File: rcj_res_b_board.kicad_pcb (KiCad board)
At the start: 2 copper layers, 82 x 100 mm, 50 parts, among them P1 M0_TERM, P10 PING0, P11 MPU9250, P12 SERVO0, P2 M1_TERM, P3 GP2Y0A41SK0F, P4 GP2Y0A41SK0F, P5 GP2Y0A41SK0F, P6 GP2Y0A41SK0F, P7 GP2Y0A21YK, P8 GP2Y0A21YK, P9 GP2Y0A21YK

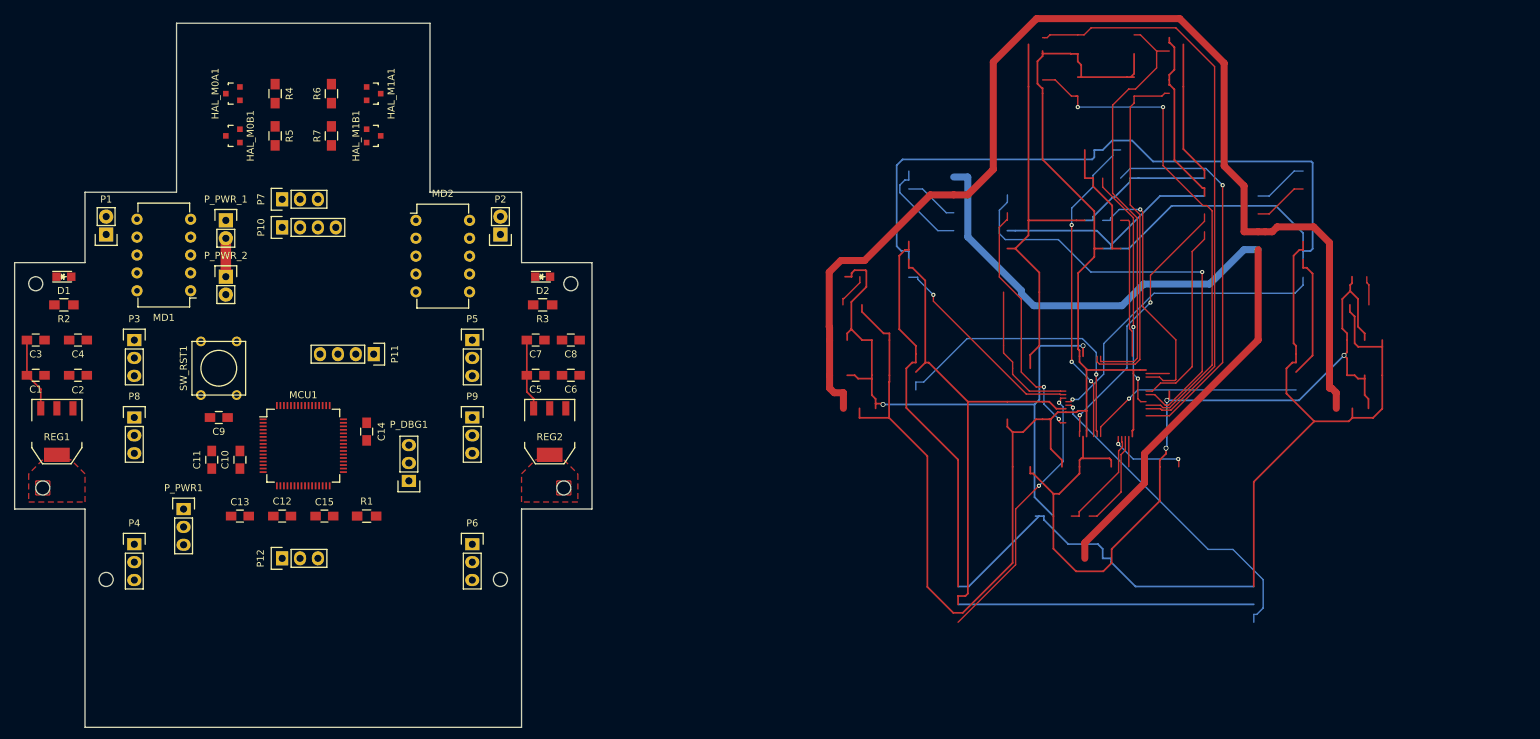
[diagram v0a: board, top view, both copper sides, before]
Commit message: Moved SMD components to back
Moving components to back to free up space -
fewer physical obstacles / limitations
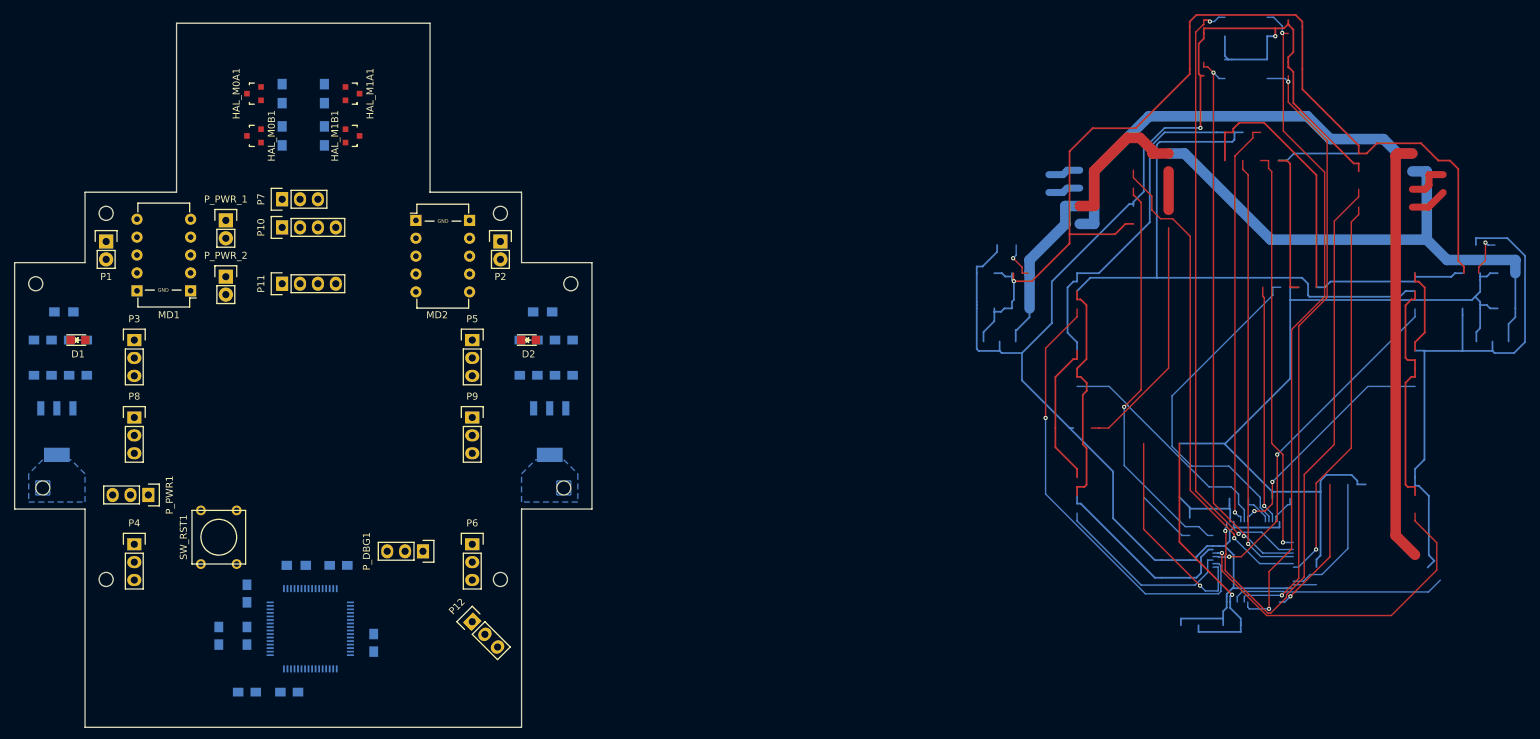
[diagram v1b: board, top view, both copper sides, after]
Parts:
- C1, C10, C11, C12, C13, C14, C15, C2, C3, C4, C5, C6, C7, C8, C9, MCU1, R1, R2, R3, R4, R5, R6, R7, REG1, REG2: moved to B.Cu
- moved C14 30.0 mm to (71.0, 138.0), turned to 90 degrees
- moved P12 28.5 mm to (85.0, 135.0), turned to 45 degrees
- moved MCU1 26.0 mm to (62.0, 136.0)
- moved C9 25.3 mm to (53.0, 131.0), turned to 90 degrees
- moved C10 25.0 mm to (53.0, 137.0), turned to 270 degrees
- moved C11 25.0 mm to (49.0, 137.0), turned to 270 degrees
- moved C12 25.0 mm to (59.0, 145.0)
- moved C13 25.0 mm to (53.0, 145.0)
- moved SW_RST1 24.0 mm to (49.0, 123.0)
- moved P11 16.4 mm to (58.0, 87.0), turned to 90 degrees
- moved R1 12.2 mm to (60.0, 127.0)
- moved P_DBG1 10.2 mm to (78.0, 125.0), turned to 270 degrees
- moved D1 9.22 mm to (29.0, 95.0)
- moved D2 9.22 mm to (93.0, 95.0)
- moved C15 7.28 mm to (66.0, 127.0)
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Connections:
- MCU1 pad 61: Net-(MCU1-Pad61) -> /SERVO0_PWM
- MD1 pad 10: Net-(MD1-Pad10) -> GNDPWR
- MD1 pad 6: GNDPWR -> Net-(MD1-Pad6)
- MD1 pad 7: VCC -> /M0_A
- MD1 pad 9: /M0_A -> VCC
- MD2 pad 10: Net-(MD2-Pad10) -> GNDPWR
- MD2 pad 6: GNDPWR -> Net-(MD2-Pad6)
- MD2 pad 7: VCC -> /M1_B
- MD2 pad 9: /M1_B -> VCC
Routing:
- net (no net): track 2290.0 -> 2540.7 mm, vias 28 -> 30
- net VCC: track 20.6 -> 0.00 mm
- net Net-(P_PWR_1-Pad2): track 5.46 -> 0.00 mm
- net GNDD: track 0.76 -> 0.00 mm
- added copper zone on B.Cu, net (none)
- removed copper zone on F.Cu, net (none)
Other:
- outline, holes or cut-outs redrawn
- board text added: "GND"

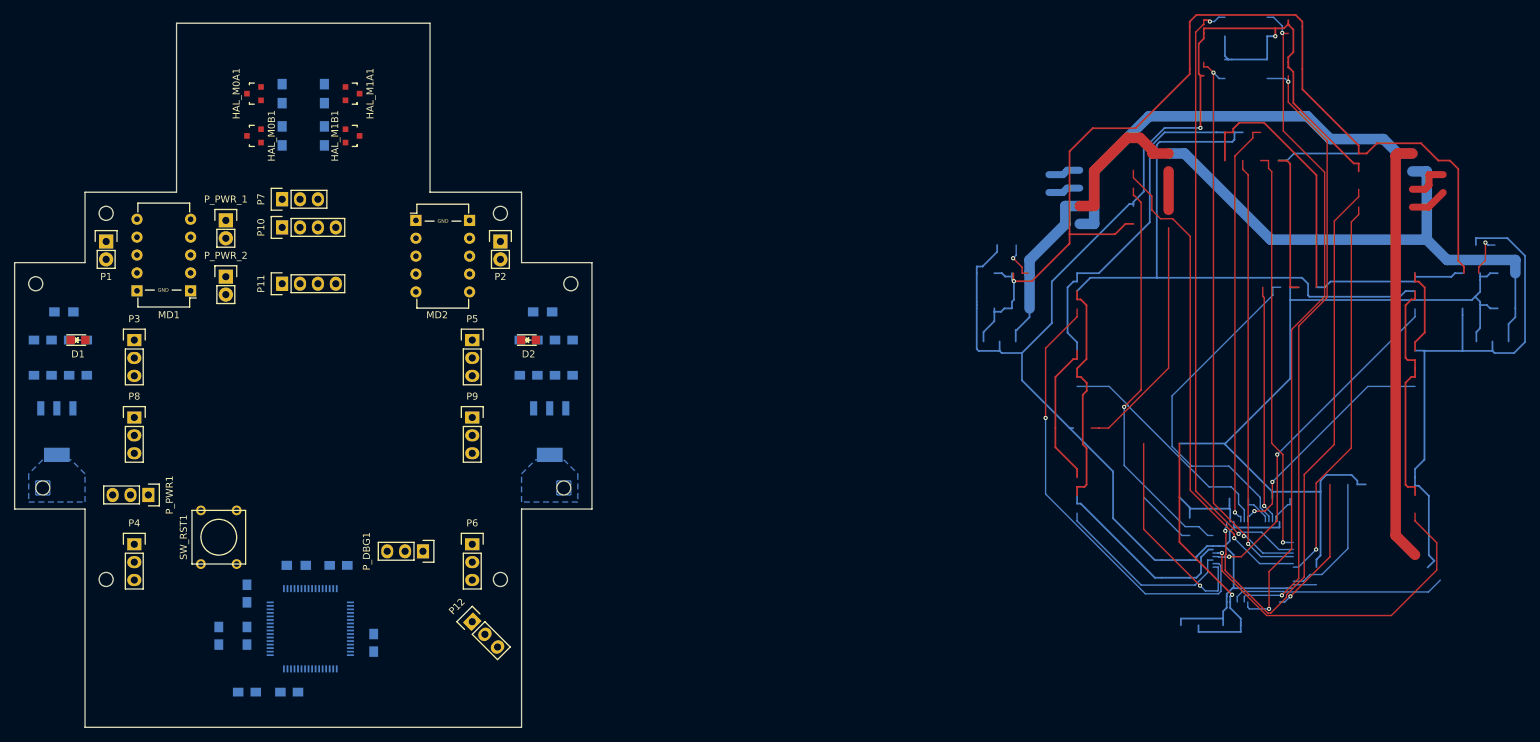
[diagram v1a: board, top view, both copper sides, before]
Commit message: General updates / improvements
Added bottom-facing IR light sensor
Changed motor driver from Pololu boards to TB6612FNG
Added OLED mount
Expanded front of board to mount motors
Added misc headers and headers for other sensors
Motor terminals are now exposed pads and not THT pin headers
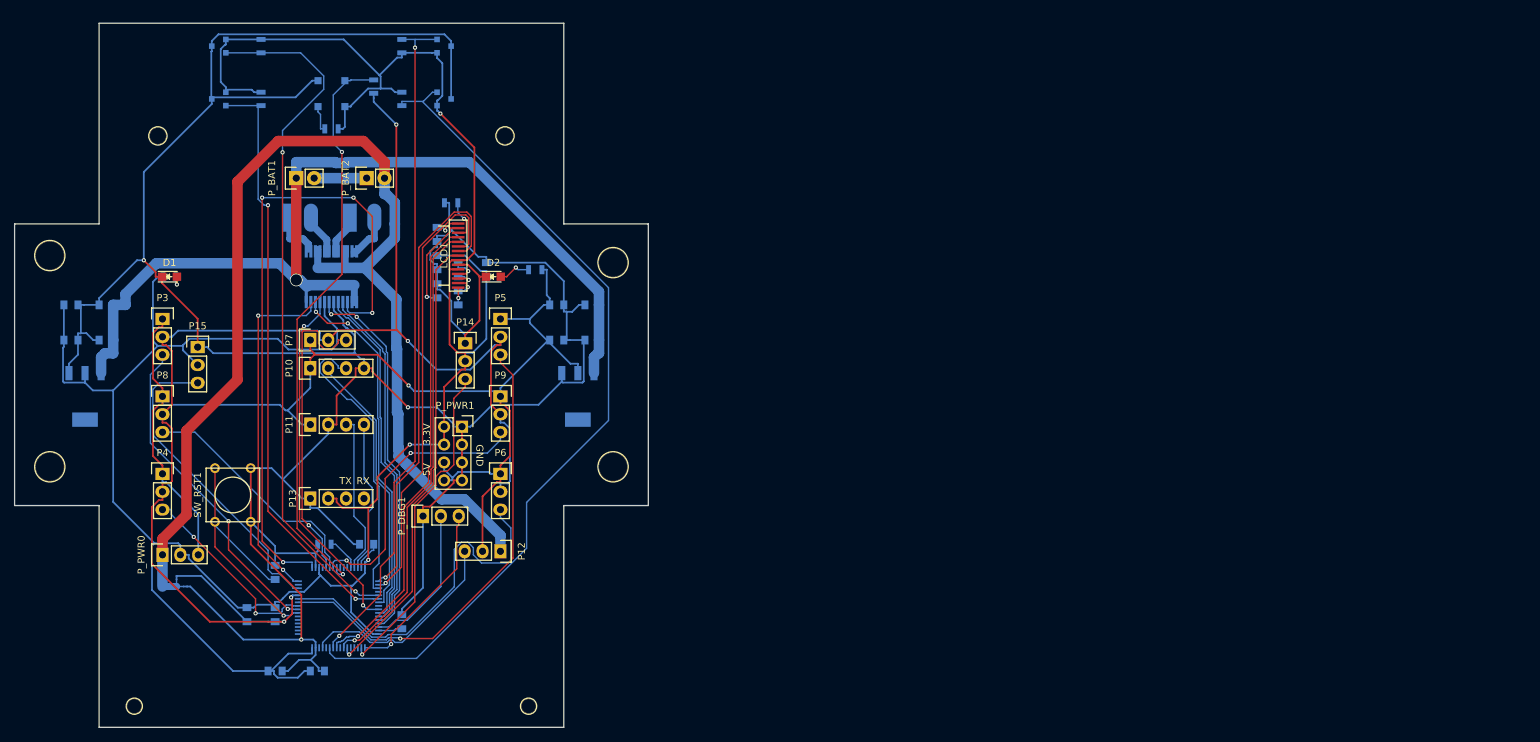
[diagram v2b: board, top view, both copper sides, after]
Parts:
- removed MD2: DRV8838-POLOLU_CARRIER, Housings_DIP:DIP-10_W7.62mm
- removed P_PWR_1, P_PWR_2: CONN_01X02, Pin_Headers:Pin_Header_Straight_1x02
- added C16: 1uF, Capacitors_SMD:C_0805, B.Cu at (83.0, 89.0)
- added C17: 1uF, Capacitors_SMD:C_0805, B.Cu at (83.0, 85.0)
- added C18: 2.2uF, Capacitors_SMD:C_0805, B.Cu at (80.0, 80.0)
- added C19: 2.2uF, Capacitors_SMD:C_0805, B.Cu at (80.0, 88.0)
- added C20: 1uF, Capacitors_SMD:C_0805, B.Cu at (80.0, 84.0)
- added C21: 1uF, Capacitors_SMD:C_0805, B.Cu at (87.0, 85.0)
- added HOLE1: 1pin, Connect:1pin, F.Cu at (25.0, 83.0)
- added HOLE2: 1pin, Connect:1pin, F.Cu at (25.0, 113.0)
- added HOLE3: 1pin, Connect:1pin, F.Cu at (105.0, 84.0)
- added HOLE4: 1pin, Connect:1pin, F.Cu at (105.0, 113.0)
- added HOLE5: 1pin, Connect:1pin, F.Cu at (37.0, 147.0)
- added HOLE6: 1pin, Connect:1pin, F.Cu at (93.0, 147.0)
- added HOLE7: 1pin, Connect:1pin, F.Cu at (40.4, 66.0)
- added HOLE8: 1pin, Connect:1pin, F.Cu at (89.7, 66.0)
- added LCD1: UG-2832HSWEG04, Custom:UG-2832HSWEG04, F.Cu at (83.0, 83.0)
- added NT1: Net_Tie, Net_Ties:NET_TIE_1.5mm, B.Cu at (74.0, 77.0)
- added NT2: Net_Tie, Net_Ties:NET_TIE_1mm, B.Cu at (42.0, 130.0)
- added NT3: Net_Tie, Net_Ties:NET_TIE_.25mm, B.Cu at (44.2, 130.0)
- added NT4: Net_Tie, Net_Ties:NET_TIE_.25mm, B.Cu at (43.0, 128.8)
- added P13: CONN_01X04, Socket_Strips:Socket_Strip_Straight_1x04, F.Cu at (62.0, 117.5)
- added P14: CONN_01X03, Socket_Strips:Socket_Strip_Straight_1x03, F.Cu at (84.0, 95.5)
- added P15: CONN_01X03, Socket_Strips:Socket_Strip_Straight_1x03, F.Cu at (46.0, 96.0)
- added P_BAT1: CONN_01X02, Socket_Strips:Socket_Strip_Straight_1x02, F.Cu at (60.0, 72.0)
- added P_BAT2: CONN_01X02, Socket_Strips:Socket_Strip_Straight_1x02, F.Cu at (70.0, 72.0)
- added P_PWR0: CONN_01X03, Socket_Strips:Socket_Strip_Straight_1x03, F.Cu at (41.0, 125.5)
- added R10: 390k, Resistors_SMD:R_0805, B.Cu at (82.0, 75.5)
- added R8: 80, Resistors_SMD:R_0805, B.Cu at (65.0, 65.0)
- added R9: 1k, Resistors_SMD:R_0805, B.Cu at (71.0, 59.0)
- added U1: OPB733TR, Custom:OPB733TR, B.Cu at (65.0, 60.0)
- C1, C10, C11, C12, C13, C14, C15, C2, C3, C4, C5, C6, C7, C8, C9: footprint Capacitors_SMD:C_0805_HandSoldering -> Capacitors_SMD:C_0805
- HAL_M0A1, HAL_M0B1, HAL_M1A1, HAL_M1B1: moved to B.Cu
- MD1: value DRV8838-POLOLU_CARRIER -> TB6612FNG; footprint Housings_DIP:DIP-10_W7.62mm -> Housings_SSOP:SSOP-24_5.3x8.2mm_Pitch0.65mm; moved to B.Cu
- P1: value M0_TERM -> CONN_01X02; footprint Pin_Headers:Pin_Header_Straight_1x02 -> Socket_Strips:Socket_Strip_Straight_1x02; moved to B.Cu
- P10, P11: footprint Pin_Headers:Pin_Header_Straight_1x04 -> Socket_Strips:Socket_Strip_Straight_1x04
- P12, P3, P4, P5, P6, P7, P8, P9, P_DBG1: footprint Pin_Headers:Pin_Header_Straight_1x03 -> Socket_Strips:Socket_Strip_Straight_1x03
- P2: value M1_TERM -> CONN_01X02; footprint Pin_Headers:Pin_Header_Straight_1x02 -> Socket_Strips:Socket_Strip_Straight_1x02; moved to B.Cu
- P_PWR1: value CONN_01X03 -> CONN_02X04; footprint Pin_Headers:Pin_Header_Straight_1x03 -> Socket_Strips:Socket_Strip_Straight_2x04
- R1, R2, R3, R4, R5, R6, R7: footprint Resistors_SMD:R_0805_HandSoldering -> Resistors_SMD:R_0805
- moved P_PWR1 45.6 mm to (83.5, 107.3)
- moved P1 26.3 mm to (59.1, 77.6)
- moved P2 21.7 mm to (67.6, 77.6)
- moved P10 20.4 mm to (62.0, 99.0), turned to 0 degrees
- moved P11 20.4 mm to (62.0, 107.0), turned to 0 degrees
- moved P7 20.4 mm to (62.0, 95.0), turned to 0 degrees
- moved MD1 20.1 mm to (65.0, 86.0), turned to 270 degrees
- moved R2 15.8 mm to (42.0, 86.0)
- moved D1 15.8 mm to (42.0, 86.0)
- moved HAL_M1A1 14.6 mm to (81.0, 53.2), turned to 90 degrees
- moved HAL_M1B1 14.0 mm to (81.0, 60.8), turned to 90 degrees
- moved R6 12.9 mm to (75.0, 53.2)
- moved R7 12.2 mm to (75.0, 60.8)
- moved P12 10.8 mm to (89.0, 125.0), turned to 180 degrees
- moved P4 10.8 mm to (41.0, 114.0), turned to 270 degrees
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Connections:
- MCU1 pad 14: Net-(MCU1-Pad14) -> /TEMP1_PWM
- MCU1 pad 16: /M0_EN -> /MD_APWM
- MCU1 pad 17: /M1_EN -> /MD_BPWM
- MCU1 pad 24: Net-(MCU1-Pad24) -> /LS_FLOOR
- MCU1 pad 33: Net-(MCU1-Pad33) -> /OLED_RST
- MCU1 pad 34: Net-(MCU1-Pad34) -> /OLED_D-C
- MCU1 pad 41: /M0_PH -> /MD_AIN1
- MCU1 pad 42: /M1_PH -> /MD_AIN2
- MCU1 pad 43: Net-(MCU1-Pad43) -> /MD_BIN1
- MCU1 pad 44: Net-(MCU1-Pad44) -> /MD_BIN2
- MCU1 pad 45: Net-(MCU1-Pad45) -> /MD_STBY
- MCU1 pad 50: Net-(MCU1-Pad50) -> /TEMP0_PWM
- MCU1 pad 54: Net-(MCU1-Pad54) -> /OLED_SS
- MCU1 pad 55: Net-(MCU1-Pad55) -> /OLED_SCLK
- MCU1 pad 57: Net-(MCU1-Pad57) -> /OLED_MOSI
- MD1 pad 1: GNDD -> Net-(MD1-Pad1)
- MD1 pad 2: /3.3V -> Net-(MD1-Pad1)
- MD1 pad 3: /M0_EN -> GNDPWR
- MD1 pad 4: /M0_PH -> GNDPWR
- MD1 pad 5: /M0_SLP -> Net-(MD1-Pad5)
- MD1 pad 6: Net-(MD1-Pad6) -> Net-(MD1-Pad5)
- MD1 pad 7: /M0_A -> Net-(MD1-Pad7)
- MD1 pad 8: /M0_B -> Net-(MD1-Pad7)
- MD1 pad 9: VCC -> GNDPWR
- P1 pad 1: /M0_A -> Net-(MD1-Pad1)
- P1 pad 2: /M0_B -> Net-(MD1-Pad5)
- P2 pad 1: /M1_A -> Net-(MD1-Pad7)
- P2 pad 2: /M1_B -> Net-(MD1-Pad11)
- P_PWR1 pad 1: GND -> GNDD
- P_PWR1 pad 3: /5V -> GNDD
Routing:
- net (no net): track 2540.7 -> 0.00 mm, vias 30 -> 0
- net GNDD: track 0.00 -> 440.7 mm, vias 0 -> 3
- net /3.3V: track 0.00 -> 376.0 mm, vias 0 -> 3
- net GNDA: track 0.00 -> 197.4 mm, vias 0 -> 4
- net /5V: track 0.00 -> 174.8 mm, vias 0 -> 1
- net VCC: track 0.00 -> 134.9 mm, vias 0 -> 1
- net /M1_ENC_B: track 0.00 -> 120.8 mm
- net /M0_ENC_A: track 0.00 -> 98.8 mm, vias 0 -> 2
- net /M1_ENC_A: track 0.00 -> 96.2 mm, vias 0 -> 2
- net /MD_BPWM: track 0.00 -> 93.2 mm, vias 0 -> 4
- net GND: track 0.00 -> 92.9 mm
- net /M0_ENC_B: track 0.00 -> 84.4 mm, vias 0 -> 2
- net /LS_FLOOR: track 0.00 -> 82.6 mm, vias 0 -> 2
- net GNDPWR: track 0.00 -> 72.2 mm
- net /OLED_MOSI: track 0.00 -> 67.4 mm, vias 0 -> 1
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- removed copper zone on B.Cu, net (none)
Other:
- board size 82 x 100 mm -> 90 x 100 mm
- board text added: "3.3V"
- board text added: "5V"
- board text added: "RX"
- board text added: "TX"
